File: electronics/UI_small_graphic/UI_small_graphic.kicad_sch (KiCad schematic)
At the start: 45 parts

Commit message: updated versionnumber, fixed DRC errors
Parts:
- BZ1: value (none) -> Buzzer; footprint (none) -> Buzzer_Beeper:Buzzer_12x9.5RM7.6
- C1, C7, C8: value (none) -> 10u; footprint (none) -> SquantorRcl:C_0603
- C2, C3: value (none) -> 1u; footprint (none) -> SquantorRcl:C_0603
- C4, C5, C6: value (none) -> 100n; footprint (none) -> SquantorRcl:C_0603
- D1, D2, D3: value (none) -> SD05; footprint (none) -> SquantorDiodes:SOD_323_onsemi
- FB1, FB2: value (none) -> 600; footprint (none) -> SquantorRcl:L_0603
- H1, H2, H3, H4: value (none) -> MountingHole; footprint (none) -> MountingHole:MountingHole_3.2mm_M3_Pad_Via
- J1: value (none) -> Conn_01x06; footprint (none) -> Connector_JST:JST_PH_S6B-PH-K_1x06_P2.00mm_Horizontal
- JP1, JP4: value (none) -> A0; footprint (none) -> SquantorSpecial:solder_jumper_0603_3way_12conn
- JP2, JP5: value (none) -> A1; footprint (none) -> SquantorSpecial:solder_jumper_0603_3way_12conn
- JP3, JP6: value (none) -> A2; footprint (none) -> SquantorSpecial:solder_jumper_0603_3way_12conn
- N1: value (none) -> OHWLOGO; footprint (none) -> Symbols:OSHW-Symbol_6.7x6mm_SilkScreen
- N2: footprint (none) -> SquantorLabels:Label_Generic
- R1, R2, R3, R5, R7, R8: value (none) -> 100; footprint (none) -> SquantorRcl:R_0603_hand
- R10, R4, R6, R9: value (none) -> 4.7K; footprint (none) -> SquantorRcl:R_0603_hand
- R11: value (none) -> TBD; footprint (none) -> SquantorRcl:R_0603_hand
- S1: value (none) -> BUT0; footprint (none) -> SquantorSwitches:Omron_B3F-4055
- S2: value (none) -> BUT1; footprint (none) -> SquantorSwitches:Omron_B3F-4055
- S3: value (none) -> BUT2; footprint (none) -> SquantorSwitches:Omron_B3F-4055
- U1: value (none) -> 128x32; footprint (none) -> SquantorModules:OLED_128x32
- U2: value (none) -> 128x64; footprint (none) -> SquantorModules:OLED_128x64
- U3: value (none) -> PCF8574; footprint (none) -> SquantorIC:SOT162-1-NXP
- U4: value (none) -> PCA9554; footprint (none) -> SquantorIC:SOT403-1-NXP

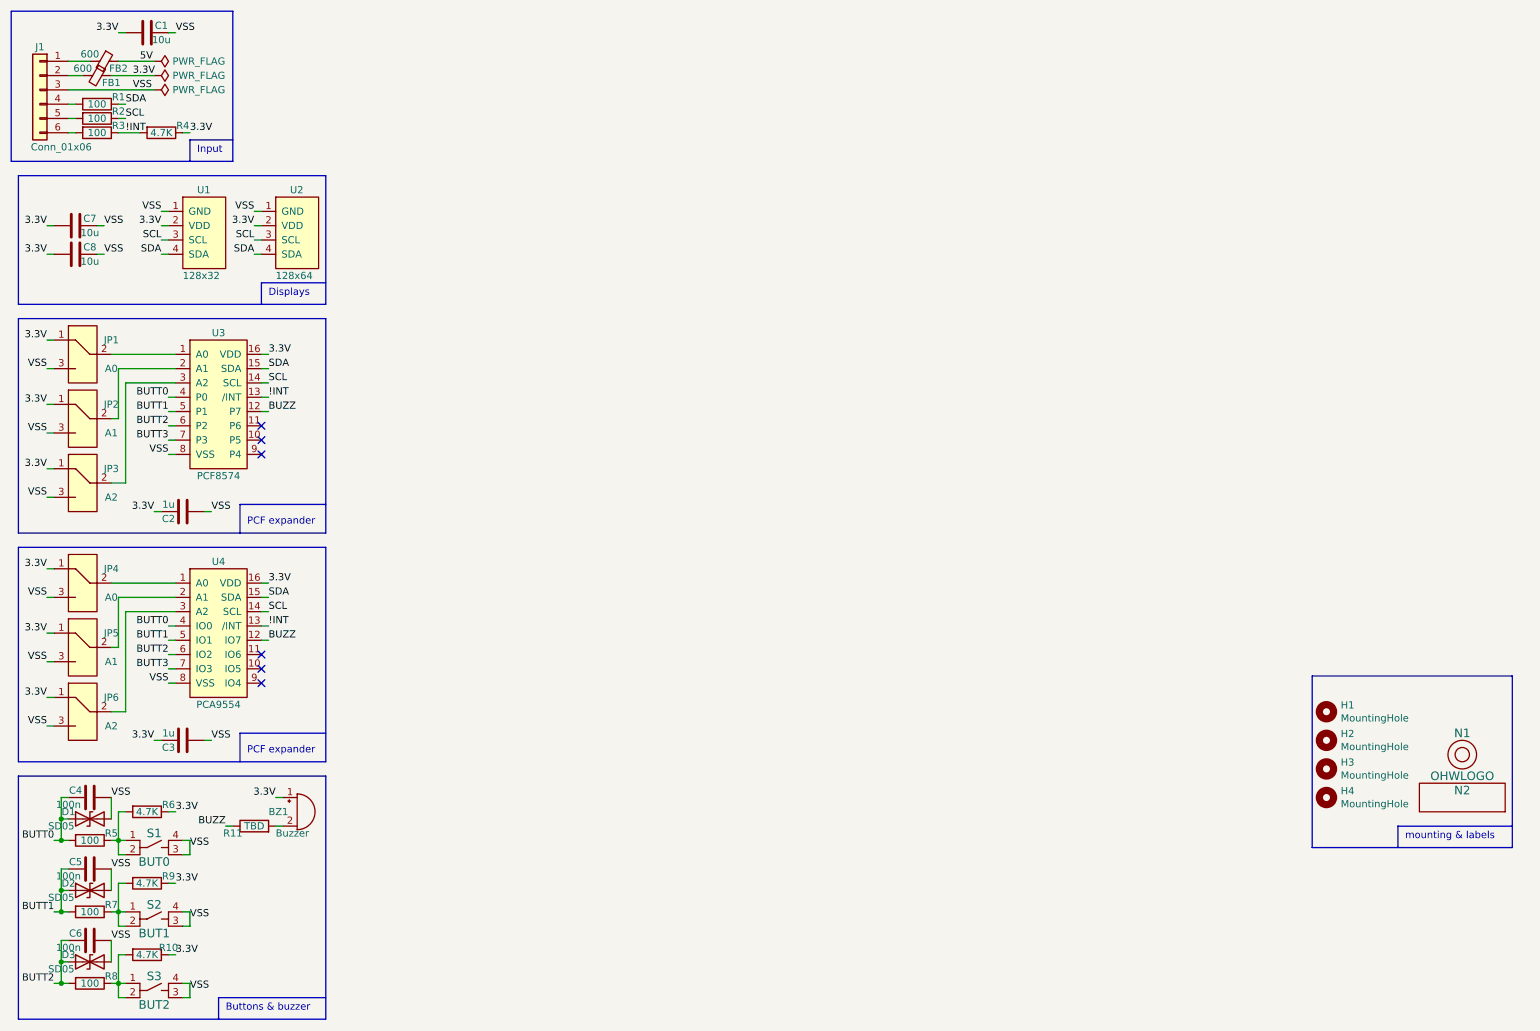
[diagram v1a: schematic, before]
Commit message: switched buttons
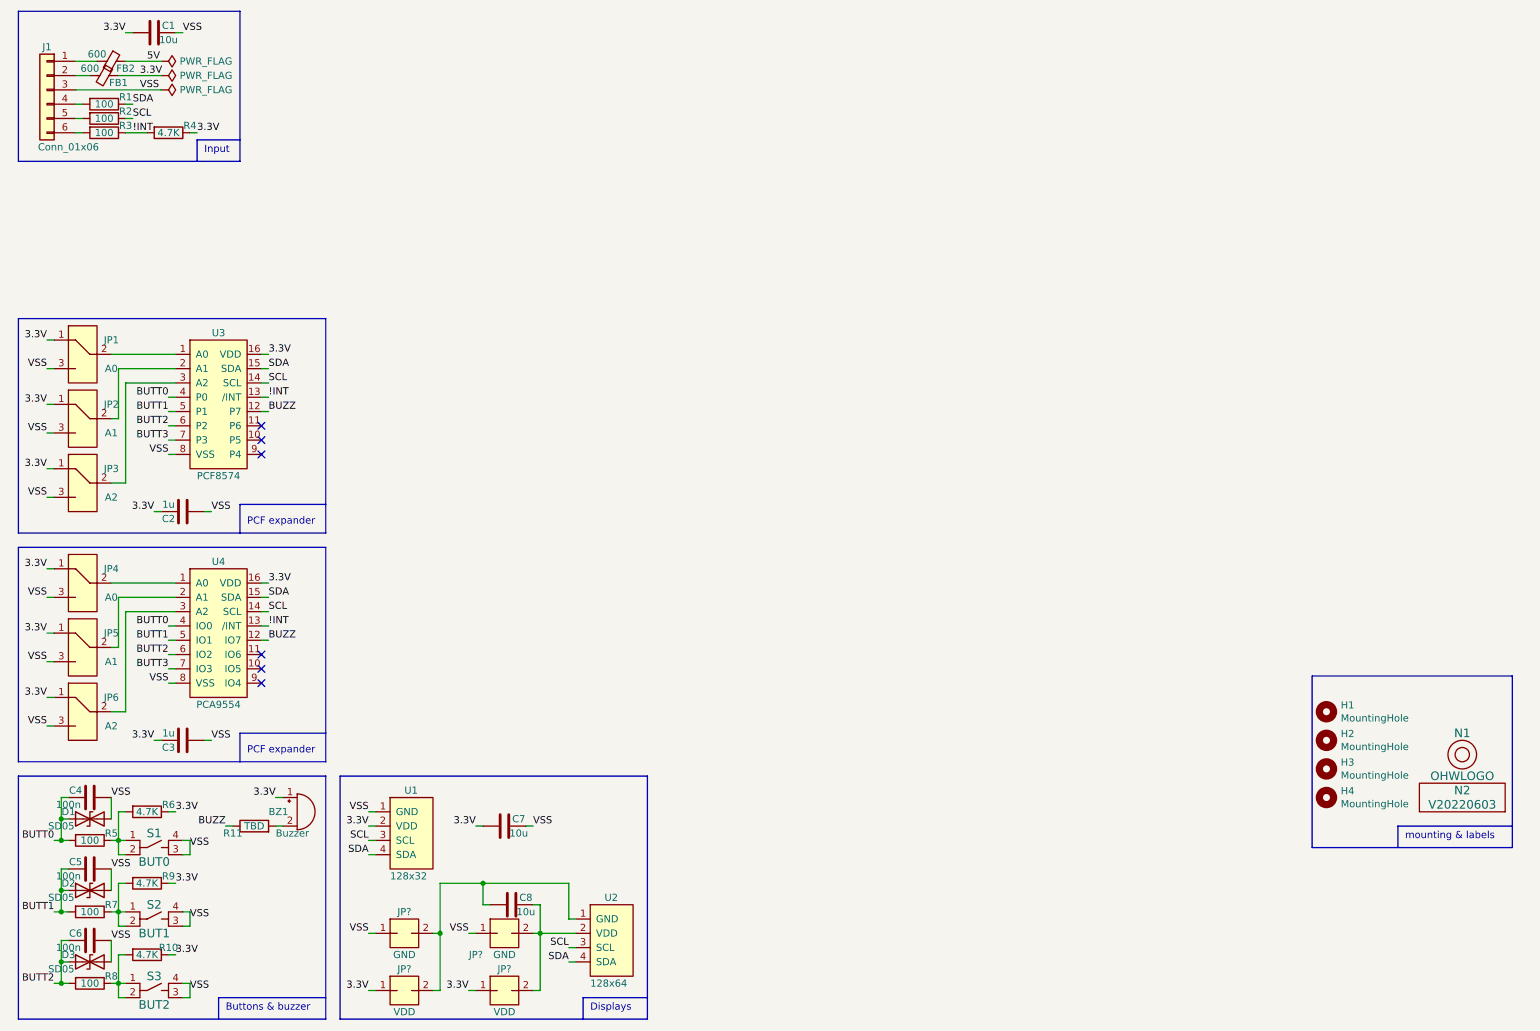
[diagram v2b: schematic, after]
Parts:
- added JP? (x2): VDD, SquantorSpecial:solder_jumper_0402_2way_noconn, symbol SquantorSpecial:Solderjumper_2way_noconn
- added JP? (x2): GND, SquantorSpecial:solder_jumper_0402_2way_noconn, symbol SquantorSpecial:Solderjumper_2way_noconn
- N2: value (none) -> V20220603
- S1, S2, S3: footprint SquantorSwitches:Omron_B3F-4055 -> SquantorSwitches:Omron_B3F-1052
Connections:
- net 3.3V: now also JP?.1, JP?.1; no longer C8.2, U2.2 (VDD)
- net VSS: now also JP?.1, JP?.1; no longer C8.1, U2.1 (GND)
- new net: C8.2, JP?.2, JP?.2, U2.1 (GND)
- new net: C8.1, JP?.2, JP?.2, U2.2 (VDD)
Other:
- moved on the sheet: C1, C7, C8, FB1, FB2, J1, R1, R2, R3, R4, U1, U2

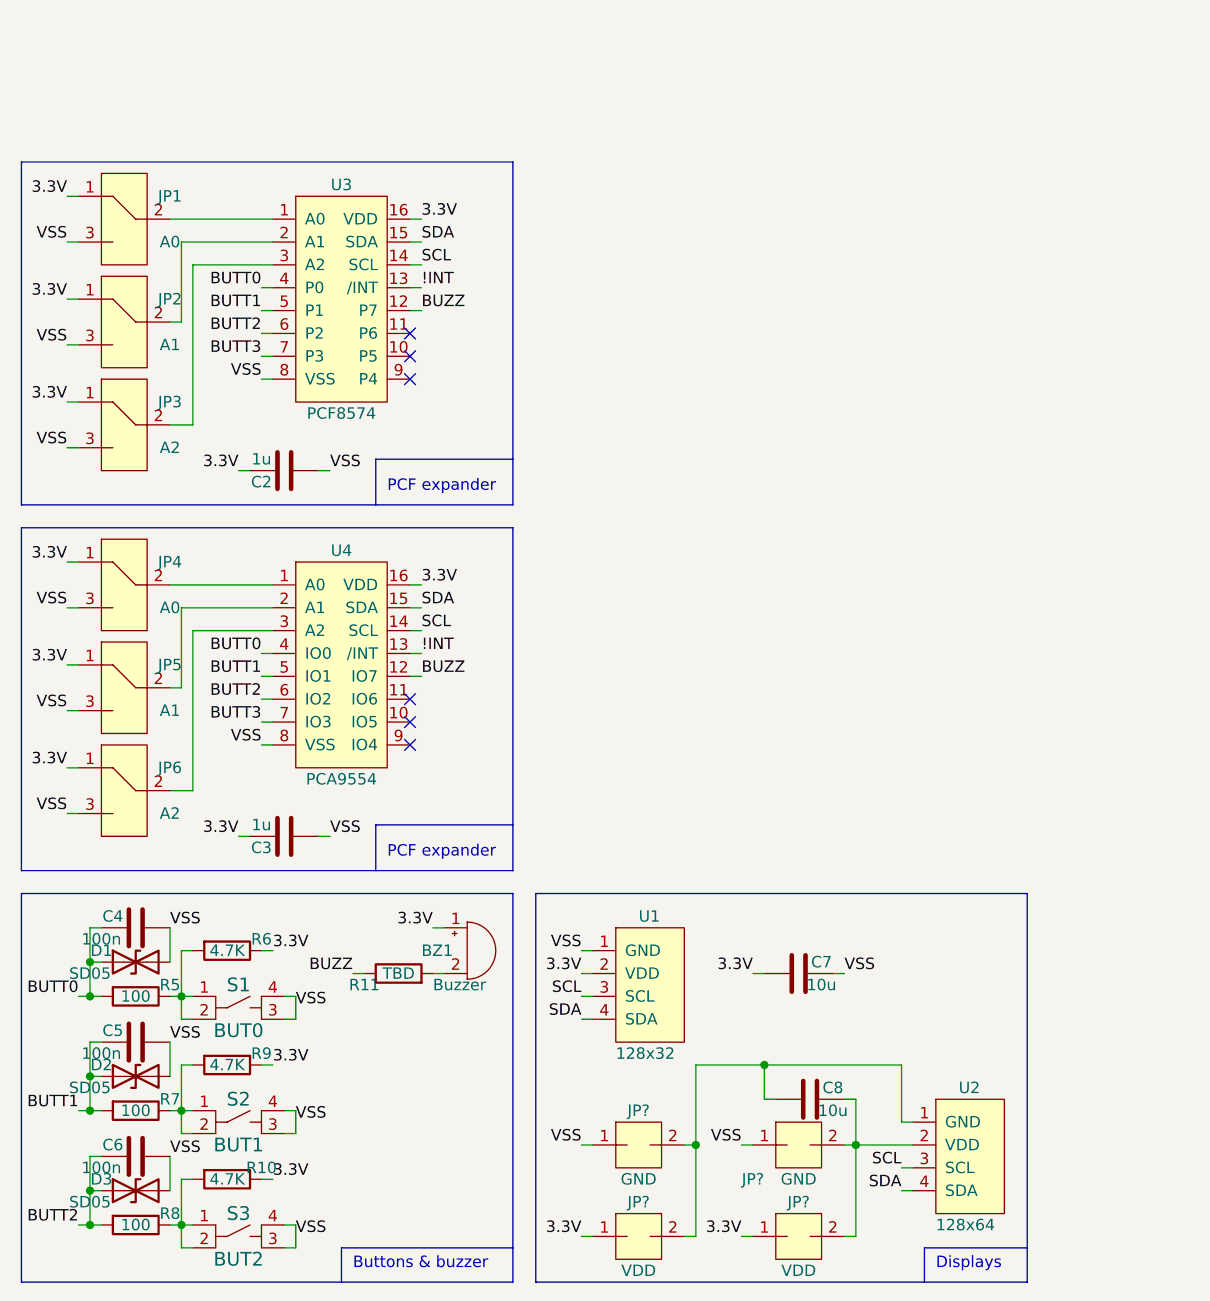
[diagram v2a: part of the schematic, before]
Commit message: added 2 buttons extra, we have space for them
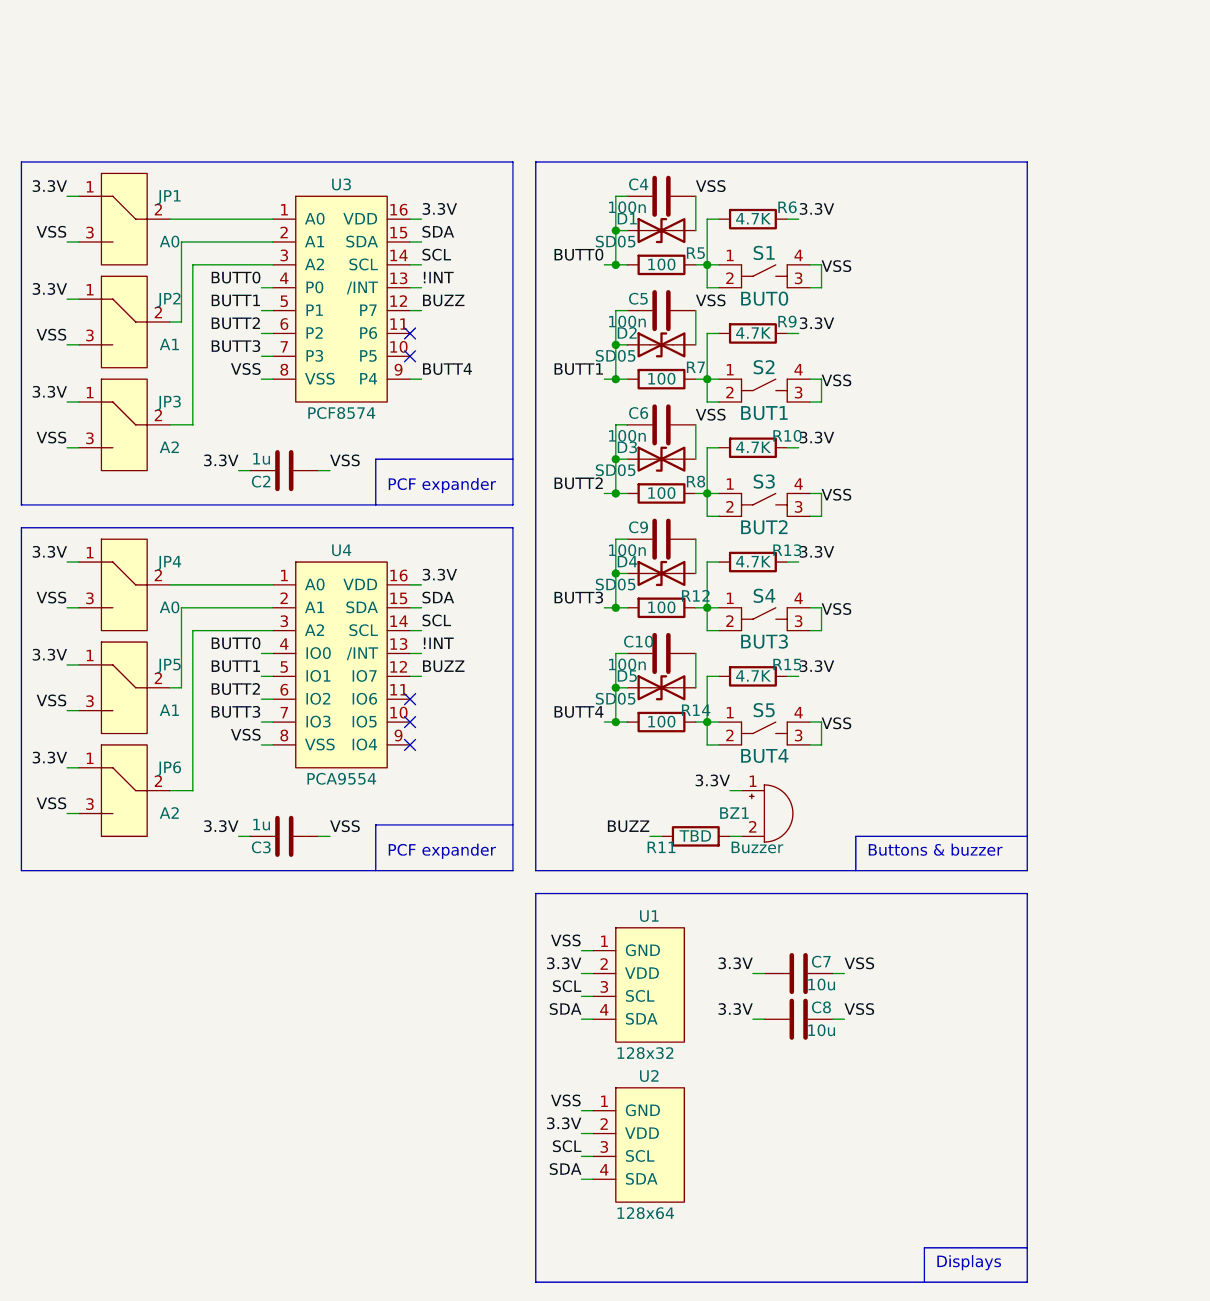
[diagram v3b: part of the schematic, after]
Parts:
- removed JP? (x2): VDD, SquantorSpecial:solder_jumper_0402_2way_noconn, symbol SquantorSpecial:Solderjumper_2way_noconn
- removed JP? (x2): GND, SquantorSpecial:solder_jumper_0402_2way_noconn, symbol SquantorSpecial:Solderjumper_2way_noconn
- added C10, C9: 100n, SquantorRcl:C_0603, symbol Device:C
- added D4, D5: SD05, SquantorDiodes:SOD_323_onsemi, symbol Device:D_TVS
- added R12, R14: 100, SquantorRcl:R_0603_hand, symbol Device:R
- added R13, R15: 4.7K, SquantorRcl:R_0603_hand, symbol Device:R
- added S4: BUT3, SquantorSwitches:Omron_B3F-1052, symbol SquantorSwitches:4pin_tact_switch
- added S5: BUT4, SquantorSwitches:Omron_B3F-1052, symbol SquantorSwitches:4pin_tact_switch
- U2: footprint SquantorModules:OLED_128x64 -> SquantorModules:OLED_132in_128x96
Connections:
- net 3.3V: now also C8.2, U2.2 (VDD), R13.1, R15.1
- net BUTT3: now also C9.1, D4.1 (A1), R12.2
- net VSS: now also C8.1, U2.1 (GND), S4.3, S4.4, S5.3, S5.4
- net BUTT4: now reaches U3.9 (P4)
- net BUTT4: now also C10.1, D5.1 (A1), R14.2
- new net: R14.1, R15.2, S5.1, S5.2
- new net: C10.2, D5.2 (A2)
- new net: C9.2, D4.2 (A2)
- new net: R12.1, R13.2, S4.1, S4.2
- no-connect marks 6 -> 5
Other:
- moved on the sheet: BZ1, C4, C5, C6, C8, D1, D2, D3, R10, R11, R5, R6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
